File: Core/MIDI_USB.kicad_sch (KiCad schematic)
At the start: 36 parts, among them J1 Conn_01x04, J4 Conn_01x06, Q3 MMBT3904, SW1 SW_Push_DPDT, SW2 SW_SPST, SW4 SW_SPST, U1 ATSAMD21G17D-A, U10 TLE9250V, U11 CAT250640VI, U12 APS1604M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

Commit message: Switch to RP2040
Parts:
- removed C3: 100nF, Capacitor_SMD:C_0603_1608Metric, symbol Device:C
- removed U1: ATSAMD21G17D-A, Package_QFP:TQFP-48_7x7mm_P0.5mm, symbol MCU_Microchip_SAMD:ATSAMD21G17D-A
- added R27, R34: 1k, Resistor_SMD:R_0603_1608Metric, symbol Device:R
- added R32, R33: 27.4, Resistor_SMD:R_0603_1608Metric, symbol Device:R
- added R35: NC, Resistor_SMD:R_0603_1608Metric, symbol Device:R
- added SW3: SW_SPST, Button_Switch_SMD:SW_SPST_B3U-1000P, symbol Switch:SW_SPST
- added U1: RP2040, Package_DFN_QFN:QFN-56-1EP_7x7mm_P0.4mm_EP3.2x3.2mm, symbol MCU_RaspberryPi:RP2040
- added U17: IS25LP032D, Package_SO:SOIC-8_3.9x4.9mm_P1.27mm, symbol Memory_Flash:AT25SF081-SSHD-X
- C4: value 100nF -> 1µF
- C41, C42: value 15pF -> 27pF
- R1: value 10k -> NC
- Y2: value 32.768kHz -> ECS-120-18-33-JGN-TR3; footprint Crystal:Crystal_SMD_EuroQuartz_EQ161-2Pin_3.2x1.5mm_HandSoldering -> Custom_FP:Crystal_SMD_3225-4Pin_3.2x2.5mm_HandSoldering; symbol Device:Crystal -> Device:Crystal_GND24
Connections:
- net +3V3: now also C5.1, R35.1, U1.1 (IOVDD), U1.10 (IOVDD), U1.22 (IOVDD), U1.33 (IOVDD), U1.42 (IOVDD), U1.43 (ADC_AVDD), U1.44 (VREG_IN), U1.48 (USB_VDD), U1.49 (IOVDD), U17.8 (VCC); no longer C1.1, C2.1, C4.1
- net CAN_INT: now also U1.15 (GPIO12)
- net CAN_SS: now also U1.12 (GPIO9)
- net EEPROM_SS: now also U1.28 (GPIO17)
- net GND: now also Y2.2, Y2.4, SW3.2 (B), U1.19 (TESTEN), U1.57 (GND), U17.4 (GND)
- net I2S_DI: now also U1.32 (GPIO21)
- net I2S_DO: now also U1.4 (GPIO2)
- net I2S_FS: now also U1.7 (GPIO5)
- net I2S_MCK: now also U1.5 (GPIO3)
- net IO_BUTT: now also U1.38 (GPIO26_ADC0)
- net LED1: now also U1.39 (GPIO27_ADC1)
- net LED2: now also U1.40 (GPIO28_ADC2)
- net RAM_SS: now also U1.31 (GPIO20)
- net RST: now also U1.26 (RUN)
- net SPI2_MISO: now also U1.27 (GPIO16)
- net SPI2_MOSI: now also U1.30 (GPIO19)
- net SPI2_SCK: now also U1.29 (GPIO18)
- net SPI_MISO: now also U1.11 (GPIO8)
- net SPI_MOSI: now also U1.14 (GPIO11)
- net SPI_SCK: now also U1.13 (GPIO10)
- net SWCLK: now also U1.24 (SWCLK)
- net SWDIO: now also U1.25 (SWD)
- net USB_D+: now also R32.1
- net USB_D-: now also R33.1
- net at C42.1: now also Y2.1, R27.1; no longer Y2.2
- net at C41.1: now also Y2.3, U1.20 (XIN); no longer Y2.1
- net at Q3.3 (C), R7.2: now also U1.41 (GPIO29_ADC3)
- new net: C1.1, C2.1, C4.1, U1.23 (DVDD), U1.45 (VREG_VOUT), U1.50 (DVDD)
- new net: R27.2, U1.21 (XOUT)
- new net: R34.2, SW3.1 (A)
- new net FLASH_CS: R34.1, R35.2, U1.56 (QSPI_SS), U17.1 (~{CS})
- new net FLASH_SCK: U1.52 (QSPI_SCLK), U17.6 (SCK)
- new net FLASH_SD0: U1.53 (QSPI_SD0), U17.5 (SI/IO0)
- new net FLASH_SD1: U1.55 (QSPI_SD1), U17.2 (SO/IO1)
- new net FLASH_SD2: U1.54 (QSPI_SD2), U17.3 (~{WP}/IO2)
- new net FLASH_SD3: U1.51 (QSPI_SD3), U17.7 (~{HOLD}/IO3)
- new net I2S_BCK: U1.6 (GPIO4)
- new net MCU_USB_D+: R32.2, U1.47 (USB_DP)
- new net MCU_USB_D-: R33.2, U1.46 (USB_DM)
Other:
- note removed: "IO button"
- note removed: "PA12 COM2[0] MOSI PA13 COM2[1] SCK PA14 COM2[2] CS PA15 COM2[3] MISO"
- note removed: "PB22 COM5[2] CS PB23 COM5[3] MISO PB02 COM5[0] MOSI PB03 COM5[1] SCK"
- moved on the sheet: C1, C15, C2, C33, C34, C35, C4, C41, C42, C5, D1, D2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

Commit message: Update metadata
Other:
- company: (none) -> GuavTek
- title: (none) -> M2IDI - USB CORE
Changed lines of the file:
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@@
 (kicad_sch (version 20230121) (generator eeschema)
   (paper "A3")
+  (title_block
+    (title "M2IDI - USB CORE")
+    (date "2023-06-18")
+    (rev "2.0")
+    (company "GuavTek")
+  )
   (junction (at 248.92 71.755) (diameter 0) (color 0 0 0 0)
   )

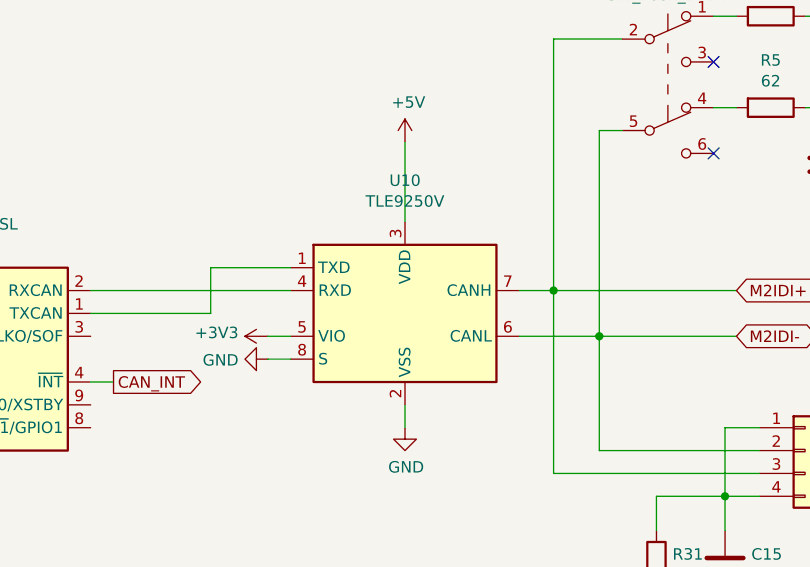
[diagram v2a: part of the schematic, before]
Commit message: Change CAN tranceiver to MCP2562
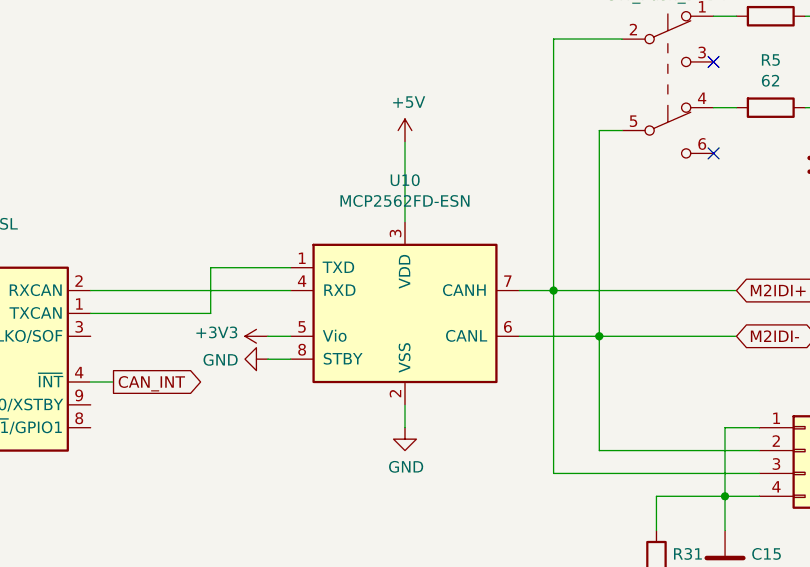
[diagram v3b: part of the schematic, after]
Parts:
- U10: value TLE9250V -> MCP2562FD-ESN; footprint Package_SO:Infineon_PG-DSO-8-27_3.9x4.9mm_EP2.65x3mm -> Package_SO:SOIC-8_3.9x4.9mm_P1.27mm; symbol Interface_CAN_LIN:MCP2558FD-xMF -> Interface_CAN_LIN:MCP2562-E-SN
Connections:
- net GND: no longer U10.9 (VSS)
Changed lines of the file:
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@@
     )
   )
-  (symbol (lib_id "Interface_CAN_LIN:MCP2558FD-xMF") (at 340.36 203.835 0) (unit 1)
+  (symbol (lib_id "Interface_CAN_LIN:MCP2562-E-SN") (at 340.36 203.835 0) (unit 1)
     (in_bom yes) (on_board yes) (dnp no)
     (property "Reference" "U10" (at 340.36 189.0776 0)
       (effects (font (size 1.27 1.27)))
     )
-    (property "Value" "TLE9250V" (at 340.36 191.389 0)
+    (property "Value" "MCP2562FD-ESN" (at 340.36 191.389 0)
       (effects (font (size 1.27 1.27)))
     )
-    (property "Footprint" "Package_SO:Infineon_PG-DSO-8-27_3.9x4.9mm_EP2.65x3mm" (at 340.36 219.075 0)
-      (effects (font (size 1.27 1.27)) hide)
+    (property "Footprint" "Package_SO:SOIC-8_3.9x4.9mm_P1.27mm" (at 340.36 216.535 0)
+      (effects (font (size 1.27 1.27) italic) hide)
     )
-    (property "Datasheet" "https://ww1.microchip.com/downloads/en/DeviceDoc/20005533A.pdf" (at 340.36 203.835 0)
+    (property "Datasheet" "http://ww1.microchip.com/downloads/en/DeviceDoc/25167A.pdf" (at 340.36 203.835 0)
       (effects (font (size 1.27 1.27)) hide)
     )
@@
     (pin "7")
     (pin "8")
-    (pin "9")
     (instances
       (project "MIDI_USB"

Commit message: Finalize module
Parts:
- C33, C34: value 15pF -> 12pF
- R4, R5: footprint Resistor_SMD:R_0603_1608Metric -> Resistor_SMD:R_0805_2012Metric
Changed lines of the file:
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@@
       (effects (font (size 1.27 1.27)))
     )
-    (property "Footprint" "Resistor_SMD:R_0603_1608Metric" (at 381 169.037 90)
+    (property "Footprint" "Resistor_SMD:R_0805_2012Metric" (at 381 169.037 90)
       (effects (font (size 1.27 1.27)) hide)
     )
@@
       (effects (font (size 1.27 1.27)))
     )
-    (property "Footprint" "Resistor_SMD:R_0603_1608Metric" (at 381 179.197 90)
+    (property "Footprint" "Resistor_SMD:R_0805_2012Metric" (at 381 179.197 90)
       (effects (font (size 1.27 1.27)) hide)
     )
@@
       (effects (font (size 1.27 1.27)))
     )
-    (property "Value" "15pF" (at 254.635 209.9056 90)
+    (property "Value" "12pF" (at 254.635 209.9056 90)
       (effects (font (size 1.27 1.27)))
     )
@@
       (effects (font (size 1.27 1.27)))
     )
-    (property "Value" "15pF" (at 254.635 220.0656 90)
-      (effects (font (size 1.27 1.27)))
-    )
+    (property "Value" "12pF" (at 254.635 220.0656 90)
+      (effects (font (size 1.27 1.27)))
+    )
